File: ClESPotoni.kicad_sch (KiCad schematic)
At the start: 47 parts, among them J1 Conn_01x06, Q1 Q_NMOS_GSD, Q2 Q_NMOS_GSD, Q3 BC817, SW1 Flash, SW2 RESET, U1 ESP32-WROOM-32, U2 DRV8833PW, U3 LD1117S33TR_SOT223

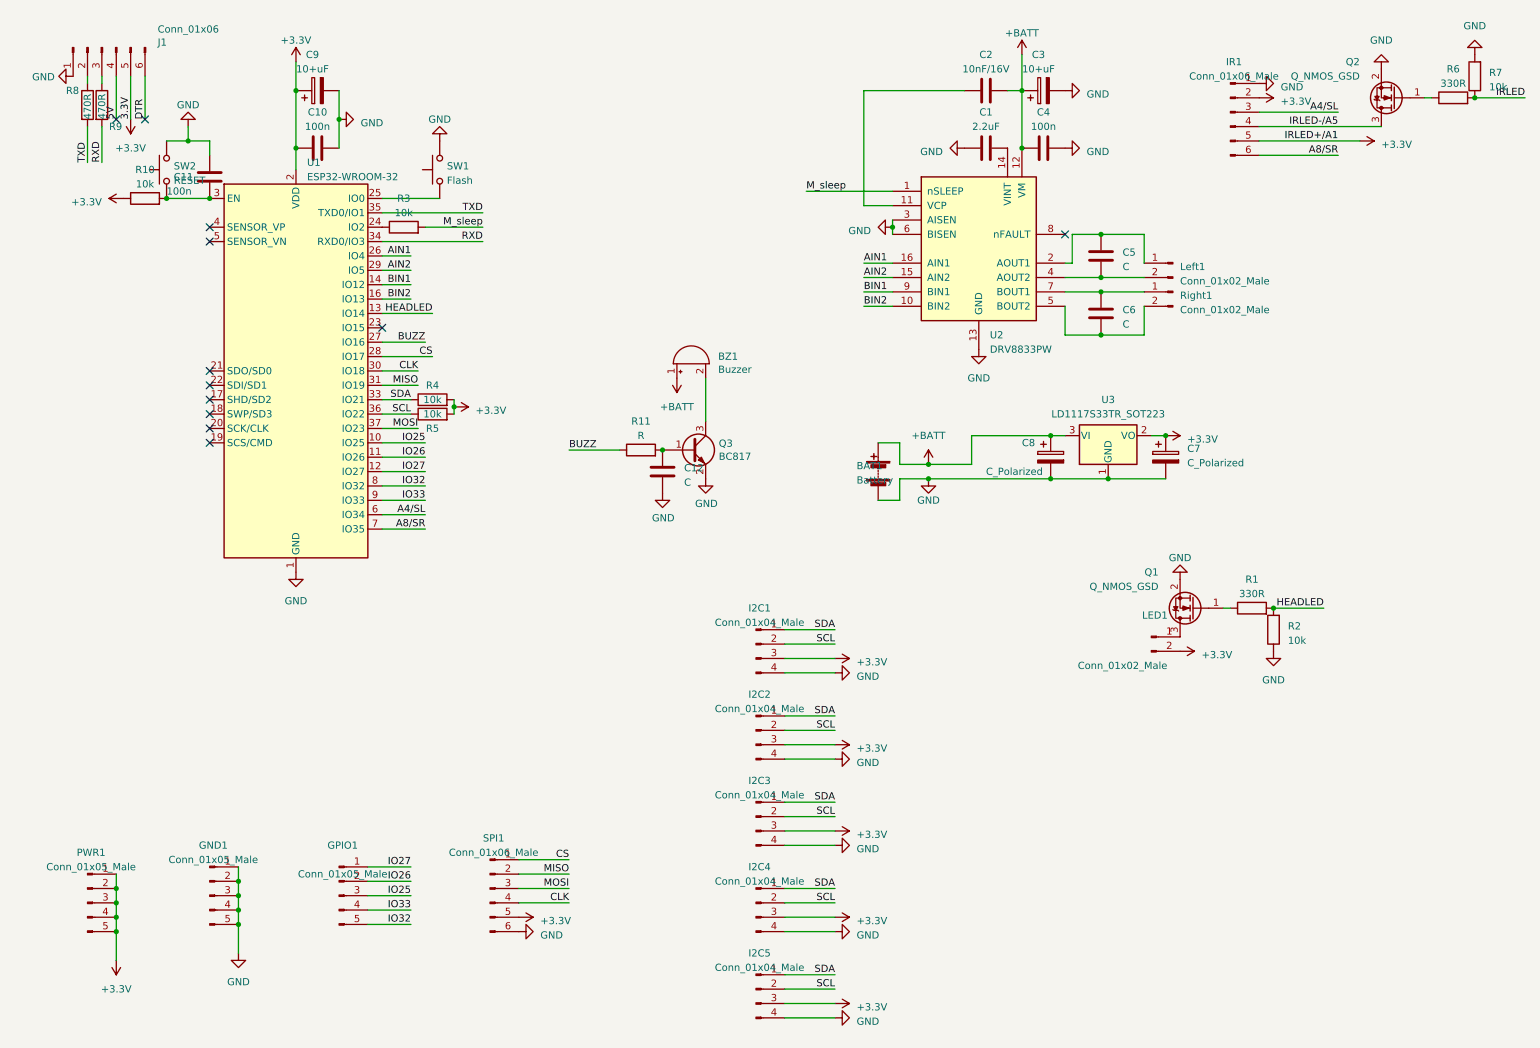
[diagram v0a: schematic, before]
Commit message: New version for ESP32-S3-WROOM-1, with bugfixes
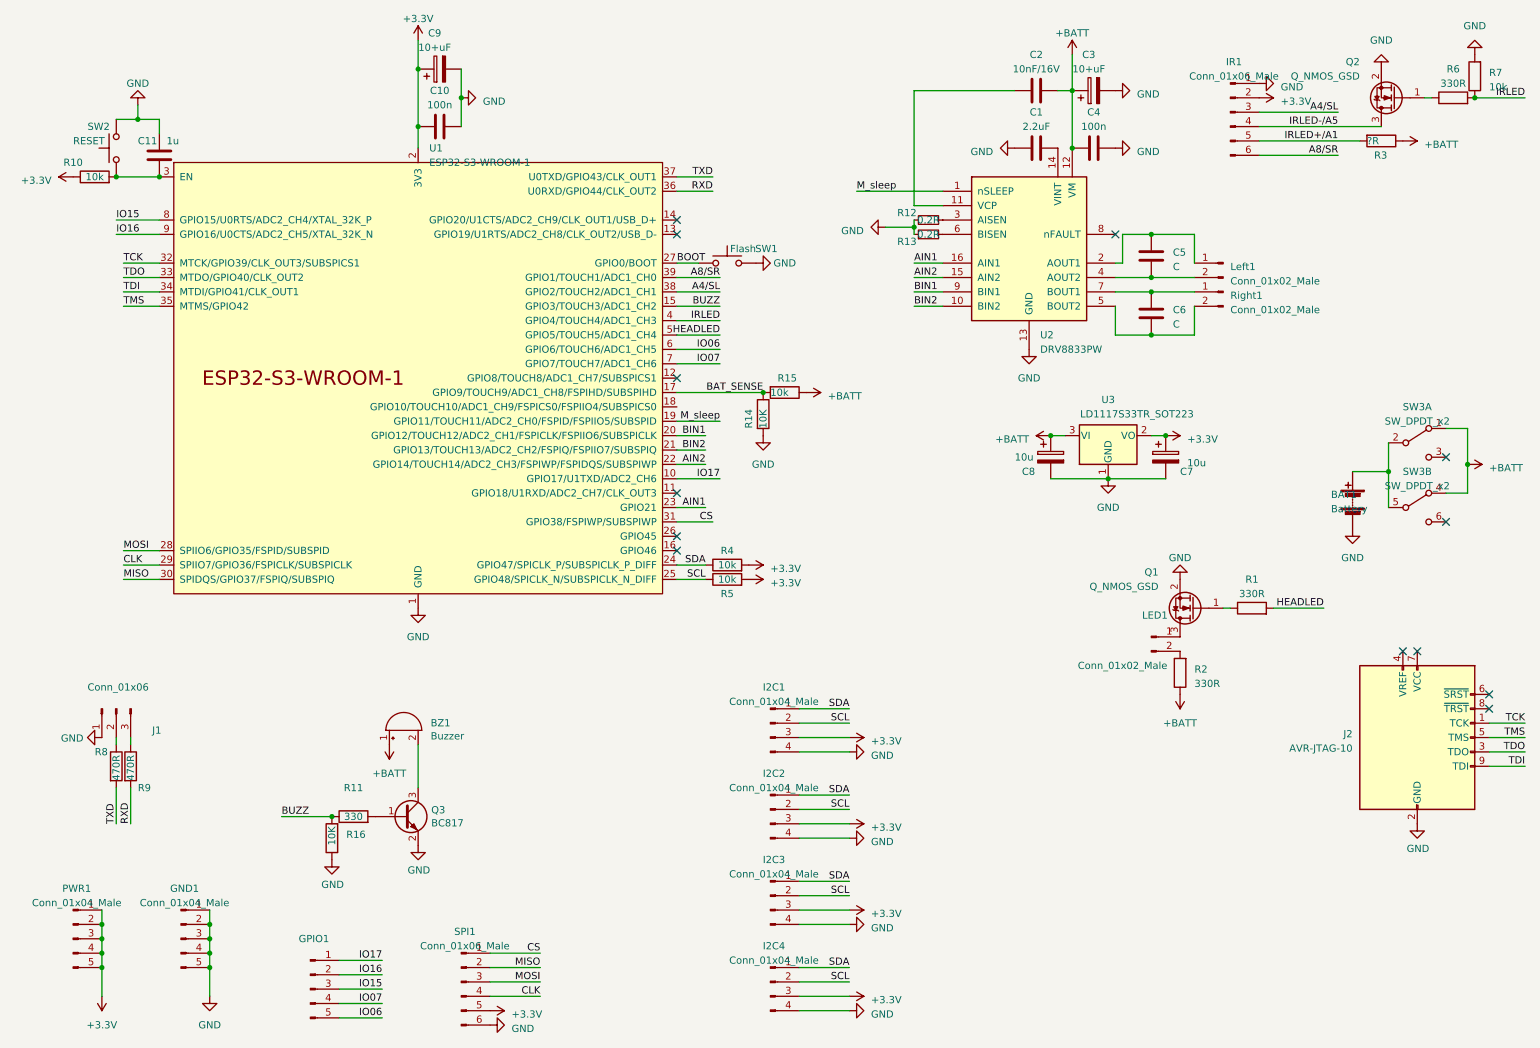
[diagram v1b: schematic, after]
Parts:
- removed C12: C, Capacitor_SMD:C_0603_1608Metric, symbol Device:C
- removed I2C5: Conn_01x04_Male, Connector_JST:JST_EH_B4B-EH-A_1x04_P2.50mm_Vertical, symbol Connector:Conn_01x04_Male
- removed U1: ESP32-WROOM-32, RF_Module:ESP32-WROOM-32, symbol RF_Module:ESP32-WROOM-32
- added J2: AVR-JTAG-10, Connector_PinHeader_1.27mm:PinHeader_2x05_P1.27mm_Vertical, symbol Connector:AVR-JTAG-10
- added R12, R13: 0.2R, Resistor_SMD:R_0603_1608Metric, symbol Device:R_Small
- added R14, R16: 10K, Resistor_SMD:R_0603_1608Metric, symbol Device:R
- added R15: 10k, Resistor_SMD:R_0603_1608Metric, symbol Device:R
- added SW3: SW_DPDT_x2, Switch_DPDT:Switch_DPDT, symbol Switch:SW_DPDT_x2
- added U1: ESP32-S3-WROOM-1, Espressif:ESP32-S3-WROOM-1, symbol Espressif:ESP32-S3-WROOM-1
- BAT1, LED1, Left1, Right1: footprint Connector_JST:JST_EH_B2B-EH-A_1x02_P2.50mm_Vertical -> Connector_JST:JST_XH_B2B-XH-AM_1x02_P2.50mm_Vertical
- C11: value 100n -> 1u
- C7, C8: value C_Polarized -> 10u
- GND1, GPIO1, PWR1: value Conn_01x05_Male -> Conn_01x04_Male; symbol Connector:Conn_01x05_Male -> Connector:Conn_01x05_Pin
- I2C1, I2C2, I2C3, I2C4: footprint Connector_JST:JST_EH_B4B-EH-A_1x04_P2.50mm_Vertical -> Connector_JST:JST_XH_B4B-XH-AM_1x04_P2.50mm_Vertical
- J1: footprint Connector_PinHeader_2.54mm:PinHeader_1x06_P2.54mm_Vertical -> Connector_PinHeader_2.54mm:PinHeader_1x03_P2.54mm_Vertical; symbol Connector:Conn_01x06_Male -> Connector:Conn_01x03_Pin
- R11: value R -> 330
- R2: value 10k -> 330R
- R3: value 10k -> ?R
- SPI1: footprint Connector_JST:JST_EH_B6B-EH-A_1x06_P2.50mm_Vertical -> Connector_JST:JST_PH_B6B-PH-K_1x06_P2.00mm_Vertical
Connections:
- net +3.3V: now also U1.2 (3V3); no longer IR1.5 (Pin_5), J1.5 (Pin_5), LED1.2 (Pin_2)
- net +BATT: now also R2.1, R3.1, R15.1, SW3.1 (A), SW3.4 (A); no longer BAT1.1 (+)
- net A4/SL: now also U1.38 (GPIO2/TOUCH2/ADC1_CH1)
- net A8/SR: now also U1.39 (GPIO1/TOUCH1/ADC1_CH0)
- net AIN1: now also U1.23 (GPIO21)
- net AIN2: now also U1.22 (GPIO14/TOUCH14/ADC2_CH3/FSPIWP/FSPIDQS/SUBSPIWP)
- net BIN1: now also U1.20 (GPIO12/TOUCH12/ADC2_CH1/FSPICLK/FSPIIO6/SUBSPICLK)
- net BIN2: now also U1.21 (GPIO13/TOUCH13/ADC2_CH2/FSPIQ/FSPIIO7/SUBSPIQ)
- net BUZZ: now also R16.2, U1.15 (GPIO3/TOUCH3/ADC1_CH2)
- net CLK: now also U1.29 (SPIIO7/GPIO36/FSPICLK/SUBSPICLK)
- net CS: now also U1.31 (GPIO38/FSPIWP/SUBSPIWP)
- net GND: now also J2.10 (GND), J2.2 (GND), R12.1, R13.1, R14.2, R16.1, U1.1 (GND), U1.40 (GND), U1.41 (GND); no longer R2.1, U2.3 (AISEN), U2.6 (BISEN)
- net HEADLED: now also U1.5 (GPIO5/TOUCH5/ADC1_CH4); no longer R2.2
- net IRLED: now also U1.4 (GPIO4/TOUCH4/ADC1_CH3)
- net MISO: now also U1.30 (SPIDQS/GPIO37/FSPIQ/SUBSPIQ)
- net MOSI: now also U1.28 (SPIIO6/GPIO35/FSPID/SUBSPID)
- net M_sleep: now also U1.19 (GPIO11/TOUCH11/ADC2_CH0/FSPID/FSPIIO5/SUBSPID); no longer R3.2
- net RXD: now also U1.36 (U0RXD/GPIO44/CLK_OUT2)
- net SCL: now also U1.25 (GPIO48/SPICLK_N/SUBSPICLK_N_DIFF)
- net SDA: now also U1.24 (GPIO47/SPICLK_P/SUBSPICLK_P_DIFF)
- net TXD: now also U1.37 (U0TXD/GPIO43/CLK_OUT1)
- net at C11.2, R10.2, SW2.1: now also U1.3 (EN)
- net BOOT: now reaches SW1.1
- net BOOT: now also U1.27 (GPIO0/BOOT)
- removed net 5V: J1.4 (Pin_4)
- removed net DTR: J1.6 (Pin_6)
- net IO25 renamed IO15
- net IO15: now also U1.8 (GPIO15/U0RTS/ADC2_CH4/XTAL_32K_P)
- net IO26 renamed IO16
- net IO16: now also U1.9 (GPIO16/U0CTS/ADC2_CH5/XTAL_32K_N)
- net IO27 renamed IO17
- net IO17: now also U1.10 (GPIO17/U1TXD/ADC2_CH6)
- net IO32 renamed IO06
- net IO06: now also U1.6 (GPIO6/TOUCH6/ADC1_CH5)
- net IO33 renamed IO07
- net IO07: now also U1.7 (GPIO7/TOUCH7/ADC1_CH6)
- new net: BAT1.1 (+), SW3.2 (B), SW3.5 (B)
- new net: R12.2, U2.3 (AISEN)
- new net: R13.2, U2.6 (BISEN)
- new net: LED1.2 (Pin_2), R2.2
- new net BAT_SENSE: R14.1, R15.2, U1.17 (GPIO9/TOUCH9/ADC1_CH8/FSPIHD/SUBSPIHD)
- new net IRLED+/A1: IR1.5 (Pin_5), R3.2
- new net TCK: J2.1 (TCK), U1.32 (MTCK/GPIO39/CLK_OUT3/SUBSPICS1)
- new net TDI: J2.9 (TDI), U1.34 (MTDI/GPIO41/CLK_OUT1)
- new net TDO: J2.3 (TDO), U1.33 (MTDO/GPIO40/CLK_OUT2)
- new net TMS: J2.5 (TMS), U1.35 (MTMS/GPIO42)
- no-connect marks 12 -> 13
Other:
- moved on the sheet: BAT1, BZ1, C1, C10, C11, C2, C3, C4, C5, C6, C9, GND1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
